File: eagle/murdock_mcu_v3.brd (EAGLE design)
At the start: 47 x 31.8 mm, 35 parts, among them IC1 MPU-9150, IC2 LT1763CS8-3.3, IC3 STM32F4XX_64, IC4 BMP085, IC5 24LC16BSN, T1 PFET, U1 USD-SOCKETNEW, X2 MURDOCK_STACK

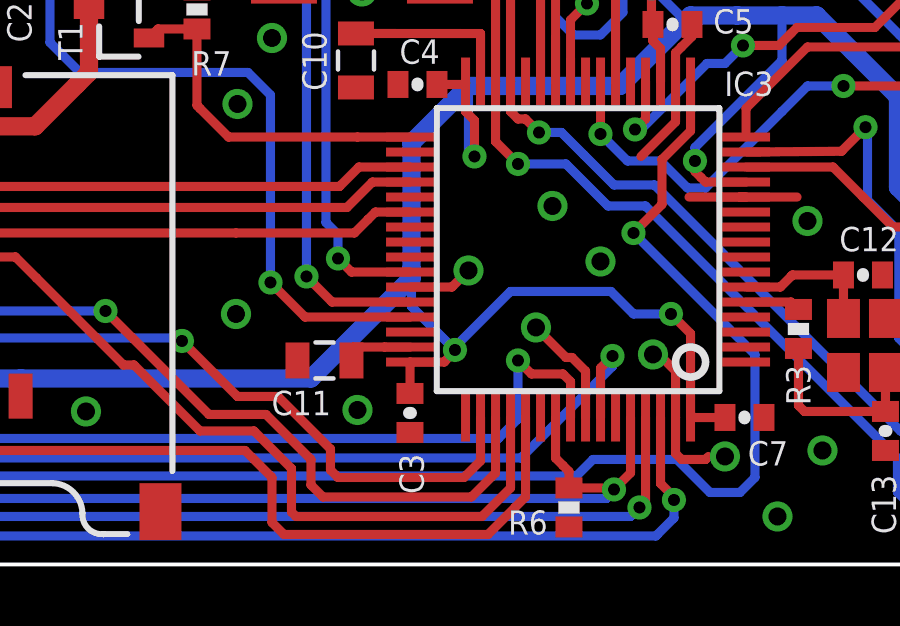
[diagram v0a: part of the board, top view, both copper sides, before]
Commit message: updated silk
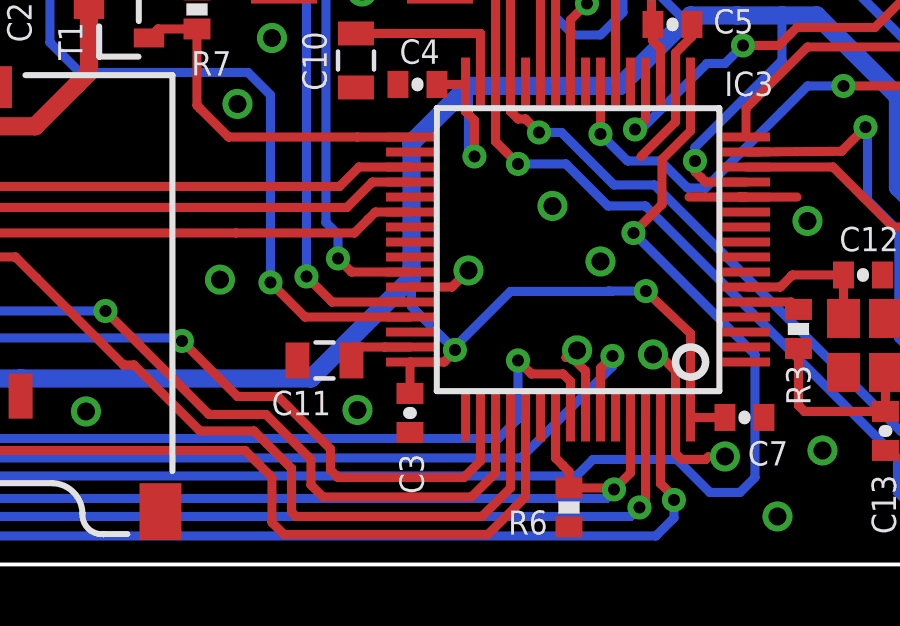
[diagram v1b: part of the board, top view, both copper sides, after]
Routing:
- net GND: track 51.9 -> 51.0 mm
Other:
- board text added: ""Technically, we're not flying...""
- board text added: "AUTOPILOT"
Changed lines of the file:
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@@
 <setting verticaltext="up"/>
 </settings>
-<grid distance="3" unitdist="mil" unit="mil" style="lines" multiple="1" display="yes" altdistance="0.025" altunitdist="inch" altunit="inch"/>
+<grid distance="3" unitdist="mil" unit="mm" style="lines" multiple="1" display="yes" altdistance="0.025" altunitdist="inch" altunit="inch"/>
 <layers>
-<layer number="1" name="Top" color="4" fill="1" visible="no" active="yes"/>
+<layer number="1" name="Top" color="4" fill="1" visible="yes" active="yes"/>
 <layer number="2" name="Route2" color="1" fill="3" visible="no" active="no"/>
 <layer number="3" name="Route3" color="4" fill="3" visible="no" active="no"/>
@@
 <layer number="14" name="Route14" color="1" fill="6" visible="no" active="no"/>
 <layer number="15" name="Route15" color="4" fill="6" visible="no" active="no"/>
-<layer number="16" name="Bottom" color="1" fill="1" visible="no" active="yes"/>
+<layer number="16" name="Bottom" color="1" fill="1" visible="yes" active="yes"/>
 <layer number="17" name="Pads" color="2" fill="1" visible="yes" active="yes"/>
 <layer number="18" name="Vias" color="2" fill="1" visible="yes" active="yes"/>
 <layer number="19" name="Unrouted" color="6" fill="1" visible="no" active="yes"/>
 <layer number="20" name="Dimension" color="15" fill="1" visible="no" active="yes"/>
-<layer number="21" name="tPlace" color="7" fill="1" visible="no" active="yes"/>
+<layer number="21" name="tPlace" color="7" fill="1" visible="yes" active="yes"/>
 <layer number="22" name="bPlace" color="7" fill="1" visible="yes" active="yes"/>
 <layer number="23" name="tOrigins" color="15" fill="1" visible="no" active="yes"/>
@@
 <wire x1="18.55" y1="23.55" x2="18.55" y2="25.7" width="0.4064" layer="21"/>
 <wire x1="12.15" y1="20.65" x2="10" y2="20.65" width="0.4064" layer="21"/>
-<text x="17.969" y="14.4804" size="1.4224" layer="22" font="vector" ratio="10" rot="MR0">MURDOCK</text>
-<text x="20.8428" y="11.3018" size="1.4224" layer="22" font="vector" ratio="10" rot="MR0">seb@exse.net</text>
+<text x="19.112" y="14.4804" size="1.4224" layer="22" font="vector" ratio="10" rot="MR0">AUTOPILOT</text>
+<text x="18.7854" y="11.2256" size="1.016" layer="22" font="vector" ratio="10" rot="MR0">seb@exse.net</text>
 <text x="11.75" y="29.35" size="0.8128" layer="22" font="vector" ratio="10" rot="MR0">SBUS/PPM</text>
 <text x="40.15" y="27.65" size="0.8128" layer="22" font="vector" ratio="10" rot="MR0">SRV1/AIL</text>
@@
 <rectangle x1="21.8313" y1="24.8031" x2="35.5473" y2="24.8793" layer="22" rot="R180"/>
 <rectangle x1="21.8313" y1="24.8793" x2="35.5473" y2="24.9555" layer="22" rot="R180"/>
+<text x="39.3192" y="7.8486" size="0.8128" layer="22" font="vector" rot="MR0">"Technically, we're not flying..."</text>
+<text x="17.969" y="17.4522" size="1.4224" layer="22" font="vector" ratio="10" rot="MR0">MURDOCK</text>
 </plain>
 <attributes>
@@
 <via x="32.45" y="10.1" extent="1-16" drill="0.6"/>
 <wire x1="39.0025" y1="12.2475" x2="37.1025" y2="12.2475" width="0.3048" layer="1"/>
-<via x="20.3" y="8.35" extent="1-16" drill="0.6"/>
+<via x="19.7666" y="9.493" extent="1-16" drill="0.6"/>
 <via x="23.95" y="21.35" extent="1-16" drill="0.6"/>
 <via x="13.35" y="28.4" extent="1-16" drill="0.6"/>
@@
 <via x="8.4" y="9.1" extent="1-16" drill="0.6"/>
 <via x="24.35" y="5.15" extent="1-16" drill="0.6"/>
-<via x="30.3" y="7.9" extent="1-16" drill="0.6"/>
+<via x="31.6716" y="7.138" extent="1-16" drill="0.6"/>
 <contactref element="IC1" pad="17"/>
 <contactref element="IC1" pad="18"/>
@@
 <wire x1="31.9525" y1="6.4475" x2="31.5" y2="6.9" width="0.3048" layer="1"/>
 <wire x1="31.5" y1="6.9" x2="31.3" y2="6.9" width="0.3048" layer="1"/>
-<wire x1="31.3" y1="6.9" x2="30.3" y2="7.9" width="0.3048" layer="1"/>
+<wire x1="31.3" y1="6.9" x2="31.6716" y2="7.138" width="0.3048" layer="1"/>
 <via x="38.35" y="1.6" extent="1-16" drill="0.6"/>
 <wire x1="34.9525" y1="15.0025" x2="34.9525" y2="14.7525" width="0.3048" layer="1"/>
@@
 <wire x1="36.5975" y1="4.8975" x2="35.4525" y2="4.8975" width="0.3048" layer="1"/>
 <wire x1="35.4525" y1="4.8975" x2="35.4525" y2="7.6975" width="0.3048" layer="1"/>
-<wire x1="35.4525" y1="7.6975" x2="34.8" y2="8.35" width="0.3048" layer="1"/>
-<via x="34.8" y="8.35" extent="1-16" drill="0.4"/>
+<wire x1="35.4525" y1="7.6975" x2="33.9618" y2="9.112" width="0.3048" layer="1"/>
+<via x="33.9618" y="9.112" extent="1-16" drill="0.4"/>
 <wire x1="4.4675" y1="21.14" x2="5.715" y2="21.1675" width="0.6096" layer="1"/>
 <wire x1="5.715" y1="21.1675" x2="5.715" y2="18.5" width="0.6096" layer="1"/>
@@
 <wire x1="27.6" y1="7.25" x2="29.45" y2="9.1" width="0.3048" layer="16"/>
 <wire x1="29.45" y1="9.1" x2="32.8" y2="9.1" width="0.3048" layer="16"/>
-<wire x1="32.8" y1="9.1" x2="33.55" y2="8.35" width="0.3048" layer="16"/>
-<wire x1="33.55" y1="8.35" x2="34.8" y2="8.35" width="0.3048" layer="16"/>
+<wire x1="32.8" y1="9.1" x2="32.7118" y2="9.112" width="0.3048" layer="16"/>
+<wire x1="32.7118" y1="9.112" x2="33.9618" y2="9.112" width="0.3048" layer="16"/>
 <wire x1="38.5" y1="23.65" x2="41.5" y2="26.65" width="0.3048" layer="16"/>
 <wire x1="41.5" y1="26.65" x2="41.5" y2="28.65" width="0.3048" layer="16"/>
